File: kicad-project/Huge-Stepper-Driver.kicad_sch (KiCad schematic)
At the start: 0 parts

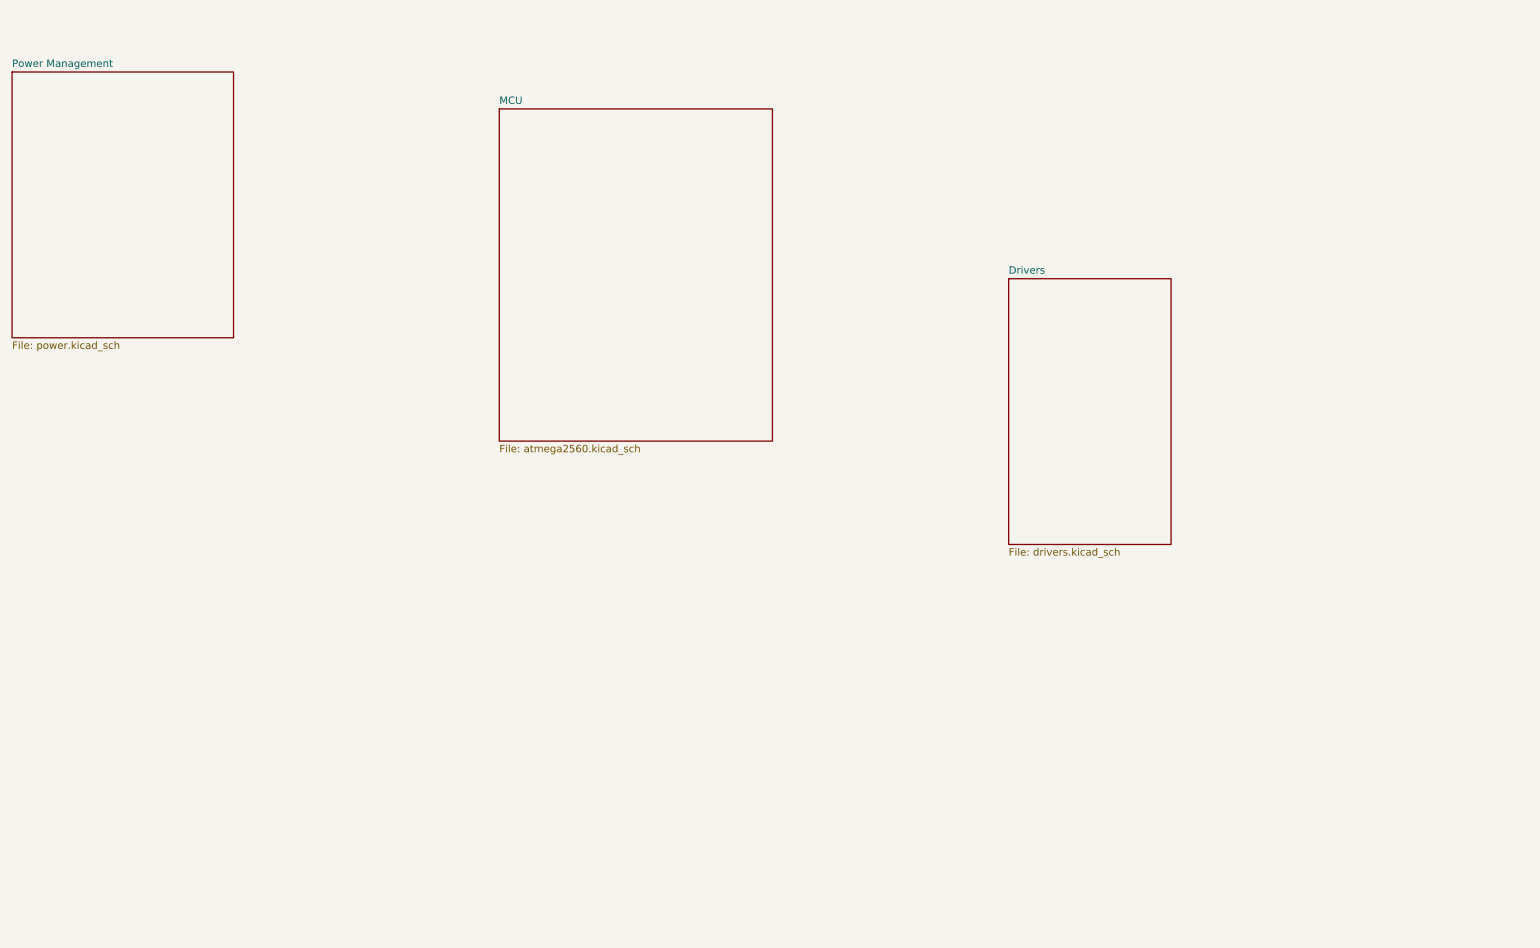
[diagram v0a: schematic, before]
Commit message: hw: rename poject and create project library
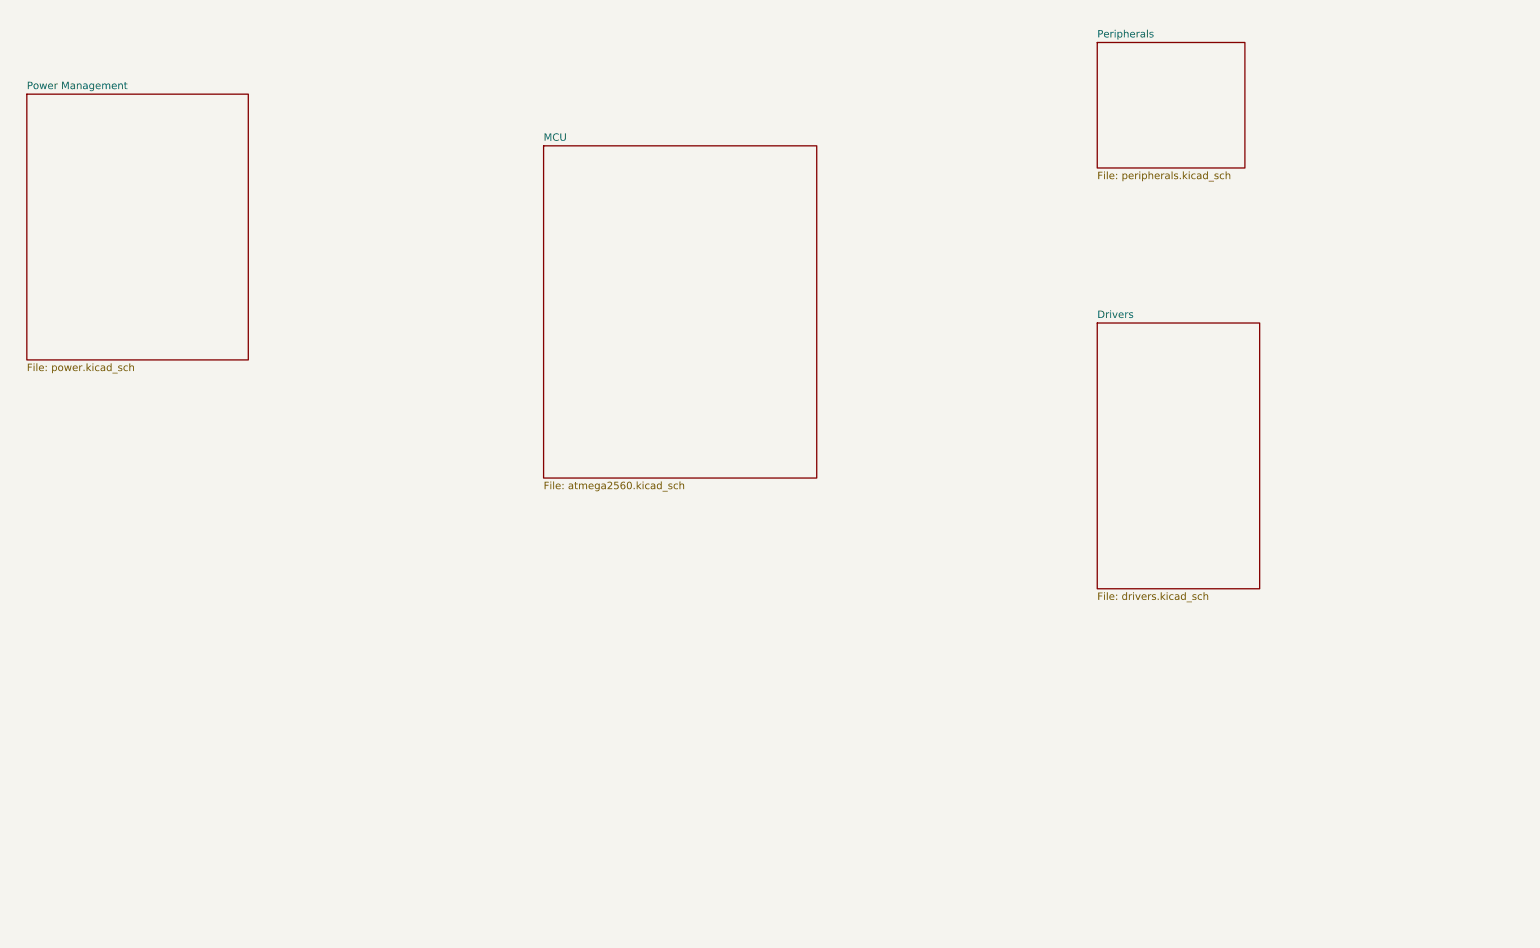
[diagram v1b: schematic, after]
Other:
- added sheet Peripherals (peripherals.kicad_sch)
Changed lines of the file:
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@@
 (kicad_sch (version 20211123) (generator eeschema)
   (paper "A4")
-  (sheet (at 119.38 52.07) (size 46.99 57.15) (fields_autoplaced)
-    (stroke (width 0.1524) (type solid) (color 0 0 0 0))
-    (fill (color 0 0 0 0.0000))
-    (property "Sheet name" "MCU" (id 0) (at 119.38 51.3584 0)
-      (effects (font (size 1.27 1.27)) (justify left bottom))
-    )
-    (property "Sheet file" "atmega2560.kicad_sch" (id 1) (at 119.38 109.8046 0)
-      (effects (font (size 1.27 1.27)) (justify left top))
-    )
-  )
-  (sheet (at 35.56 45.72) (size 38.1 45.72) (fields_autoplaced)
-    (stroke (width 0.1524) (type solid) (color 0 0 0 0))
-    (fill (color 0 0 0 0.0000))
-    (property "Sheet name" "Power Management" (id 0) (at 35.56 45.0084 0)
-      (effects (font (size 1.27 1.27)) (justify left bottom))
-    )
-    (property "Sheet file" "power.kicad_sch" (id 1) (at 35.56 92.0246 0)
-      (effects (font (size 1.27 1.27)) (justify left top))
-    )
-  )
-  (sheet (at 207.01 81.28) (size 27.94 45.72) (fields_autoplaced)
-    (stroke (width 0.1524) (type solid) (color 0 0 0 0))
-    (fill (color 0 0 0 0.0000))
-    (property "Sheet name" "Drivers" (id 0) (at 207.01 80.5684 0)
-      (effects (font (size 1.27 1.27)) (justify left bottom))
-    )
-    (property "Sheet file" "drivers.kicad_sch" (id 1) (at 207.01 127.5846 0)
+  (sheet (at 127 58.42) (size 46.99 57.15) (fields_autoplaced)
+    (stroke (width 0.1524) (type solid) (color 0 0 0 0))
+    (fill (color 0 0 0 0.0000))
+    (property "Sheet name" "MCU" (id 0) (at 127 57.7084 0)
+      (effects (font (size 1.27 1.27)) (justify left bottom))
+    )
+    (property "Sheet file" "atmega2560.kicad_sch" (id 1) (at 127 116.1546 0)
+      (effects (font (size 1.27 1.27)) (justify left top))
+    )
+  )
+  (sheet (at 222.25 40.64) (size 25.4 21.59) (fields_autoplaced)
+    (stroke (width 0.1524) (type solid) (color 0 0 0 0))
+    (fill (color 0 0 0 0.0000))
+    (property "Sheet name" "Peripherals" (id 0) (at 222.25 39.9284 0)
+      (effects (font (size 1.27 1.27)) (justify left bottom))
+    )
+    (property "Sheet file" "peripherals.kicad_sch" (id 1) (at 222.25 62.8146 0)
+      (effects (font (size 1.27 1.27)) (justify left top))
+    )
+  )
+  (sheet (at 38.1 49.53) (size 38.1 45.72) (fields_autoplaced)
+    (stroke (width 0.1524) (type solid) (color 0 0 0 0))
+    (fill (color 0 0 0 0.0000))
+    (property "Sheet name" "Power Management" (id 0) (at 38.1 48.8184 0)
+      (effects (font (size 1.27 1.27)) (justify left bottom))
+    )
+    (property "Sheet file" "power.kicad_sch" (id 1) (at 38.1 95.8346 0)
+      (effects (font (size 1.27 1.27)) (justify left top))
+    )
+  )
+  (sheet (at 222.25 88.9) (size 27.94 45.72) (fields_autoplaced)
+    (stroke (width 0.1524) (type solid) (color 0 0 0 0))
+    (fill (color 0 0 0 0.0000))
+    (property "Sheet name" "Drivers" (id 0) (at 222.25 88.1884 0)
+      (effects (font (size 1.27 1.27)) (justify left bottom))
+    )
+    (property "Sheet file" "drivers.kicad_sch" (id 1) (at 222.25 135.2046 0)
       (effects (font (size 1.27 1.27)) (justify left top))
     )
@@
     (path "/f5d928fb-e6dd-4010-8c57-6f8716fdab33" (page "3"))
     (path "/4f8c7c93-1d61-4a01-a5c2-288dd81060c9" (page "4"))
+    (path "/3d25ea00-3597-4b84-9896-d06c9254cef7" (page "5"))
   )
   (symbol_instances
@@
       (reference "#PWR?") (unit 1) (value "+5V") (footprint "")
     )
+    (path "/f5d928fb-e6dd-4010-8c57-6f8716fdab33/25a53107-0414-4363-9616-a7d291dc0d84"
+      (reference "#PWR?") (unit 1) (value "+12V") (footprint "")
+    )
     (path "/f5d928fb-e6dd-4010-8c57-6f8716fdab33/2942b730-6142-444d-941a-095db45b9805"
       (reference "#PWR?") (unit 1) (value "GND") (footprint "")
@@
       (reference "#PWR?") (unit 1) (value "+5V") (footprint "")
     )
+    (path "/3d25ea00-3597-4b84-9896-d06c9254cef7/4c436fb9-5de1-4241-82c9-60c46b745983"
+      (reference "#PWR?") (unit 1) (value "GND") (footprint "")
+    )
+    (path "/3d25ea00-3597-4b84-9896-d06c9254cef7/53eb5fc0-41cc-43ad-8003-3a7163adca82"
+      (reference "#PWR?") (unit 1) (value "GND") (footprint "")
+    )
+    (path "/3d25ea00-3597-4b84-9896-d06c9254cef7/5b7004c0-970a-4c32-afa1-b9c30b457ebb"
+      (reference "#PWR?") (unit 1) (value "GND") (footprint "")
+    )
     (path "/f5d928fb-e6dd-4010-8c57-6f8716fdab33/5f7cd6da-1976-40d7-8175-57317f64748c"
       (reference "#PWR?") (unit 1) (value "GND") (footprint "")
     )
+    (path "/3d25ea00-3597-4b84-9896-d06c9254cef7/756c57ca-b724-416e-bbc3-080fcadffb70"
+      (reference "#PWR?") (unit 1) (value "GND") (footprint "")
+    )
+    (path "/f5d928fb-e6dd-4010-8c57-6f8716fdab33/9a7047f9-acea-486f-a364-b7368cdd257a"
+      (reference "#PWR?") (unit 1) (value "+12V") (footprint "")
+    )
     (path "/18df3b4d-b69d-45aa-8b2a-e433af4ece2d/a7d63353-8f9e-4f12-a0a0-581ff55f9e74"
       (reference "#PWR?") (unit 1) (value "GND") (footprint "")
     )
+    (path "/3d25ea00-3597-4b84-9896-d06c9254cef7/aede887e-5713-4410-b301-8003185f738f"
+      (reference "#PWR?") (unit 1) (value "GND") (footprint "")
+    )
     (path "/f5d928fb-e6dd-4010-8c57-6f8716fdab33/bd1d99b9-625b-4d9f-8b97-620535fb200d"
       (reference "#PWR?") (unit 1) (value "GND") (footprint "")
+    )
+    (path "/3d25ea00-3597-4b84-9896-d06c9254cef7/c6a9b2da-bd30-4983-ad00-dc03e640a581"
+      (reference "#PWR?") (unit 1) (value "+3V3") (footprint "")
+    )
+    (path "/3d25ea00-3597-4b84-9896-d06c9254cef7/cefd0a94-cc8a-494c-9a46-c853604e1e17"
+      (reference "#PWR?") (unit 1) (value "+3V3") (footprint "")
+    )
+    (path "/3d25ea00-3597-4b84-9896-d06c9254cef7/d190d7a3-7bf5-42db-8c6f-15b2790a1189"
+      (reference "#PWR?") (unit 1) (value "GND") (footprint "")
+    )
+    (path "/3d25ea00-3597-4b84-9896-d06c9254cef7/e22a8115-21c4-4079-b548-13d39057d641"
+      (reference "#PWR?") (unit 1) (value "+3V3") (footprint "")
     )
     (path "/f5d928fb-e6dd-4010-8c57-6f8716fdab33/e24fb780-68ae-495b-a949-7ef7931dd25d"
@@
       (reference "#PWR?") (unit 1) (value "GND") (footprint "")
     )
+    (path "/3d25ea00-3597-4b84-9896-d06c9254cef7/80dec395-b03d-42e4-894e-d6e2d9479fc8"
+      (reference "BZ?") (unit 1) (value "Buzzer") (footprint "Buzzer_Beeper:Buzzer_12x9.5RM7.6")
+    )
     (path "/f5d928fb-e6dd-4010-8c57-6f8716fdab33/38c76cd1-d3ed-4a45-9878-1458ed9b04ed"
       (reference "C?") (unit 1) (value "0.1u") (footprint "")
@@
       (reference "C?") (unit 1) (value "0.1u") (footprint "")
     )
+    (path "/3d25ea00-3597-4b84-9896-d06c9254cef7/716e5416-b330-423a-811f-046a4ee64f5e"
+      (reference "D?") (unit 1) (value "GREEN_LED") (footprint "LED_SMD:LED_0603_1608Metric")
+    )
+    (path "/3d25ea00-3597-4b84-9896-d06c9254cef7/e30e2336-2dbc-4130-9889-d5f2eae65709"
+      (reference "D?") (unit 1) (value "LED_RGB") (footprint "LED_SMD:LED_RGB_1210")
+    )
     (path "/4f8c7c93-1d61-4a01-a5c2-288dd81060c9/41d2c036-0133-4858-af37-ae05a7f175e8"
       (reference "H?") (unit 1) (value "MountingHole") (footprint "")
@@
       (reference "J?") (unit 1) (value "Screw_Terminal_01x02") (footprint "")
     )
+    (path "/3d25ea00-3597-4b84-9896-d06c9254cef7/4e3ce3b2-0062-4894-90c9-d123f1516483"
+      (reference "J?") (unit 1) (value "Conn_01x04") (footprint "Connector_PinHeader_2.54mm:PinHeader_1x04_P2.54mm_Vertical_SMD_Pin1Left")
+    )
+    (path "/f5d928fb-e6dd-4010-8c57-6f8716fdab33/70d8d5c4-6ca3-4d9d-b0ee-1b92bdb07be0"
+      (reference "J?") (unit 1) (value "Screw_Terminal_01x05") (footprint "TerminalBlock_TE-Connectivity:TerminalBlock_TE_282834-5_1x05_P2.54mm_Horizontal")
+    )
+    (path "/f5d928fb-e6dd-4010-8c57-6f8716fdab33/9e493dfe-75da-48fa-ad61-eaa217b673f3"
+      (reference "J?") (unit 1) (value "Screw_Terminal_01x05") (footprint "TerminalBlock_TE-Connectivity:TerminalBlock_TE_282834-5_1x05_P2.54mm_Horizontal")
+    )
+    (path "/3d25ea00-3597-4b84-9896-d06c9254cef7/b93ddd20-6b06-4f50-a42d-38095b2ae703"
+      (reference "Q?") (unit 1) (value "PDTC114Y") (footprint "")
+    )
     (path "/f5d928fb-e6dd-4010-8c57-6f8716fdab33/37dac4eb-1daa-4fa2-a92f-452234732f13"
       (reference "R?") (unit 1) (value "R") (footprint "")
     )
+    (path "/3d25ea00-3597-4b84-9896-d06c9254cef7/3a40cb9a-6096-4b48-bae2-62ca7cd7dbcd"
+      (reference "R?") (unit 1) (value "R") (footprint "Resistor_SMD:R_0603_1608Metric")
+    )
     (path "/f5d928fb-e6dd-4010-8c57-6f8716fdab33/3e5f1652-1224-4863-9681-d782bc9660ba"
       (reference "R?") (unit 1) (value "5k") (footprint "")
     )
+    (path "/3d25ea00-3597-4b84-9896-d06c9254cef7/476016a1-85a2-490a-9e22-631280b45f0e"
+      (reference "R?") (unit 1) (value "4k7") (footprint "Resistor_SMD:R_0603_1608Metric")
+    )
     (path "/f5d928fb-e6dd-4010-8c57-6f8716fdab33/62c00295-c371-40ec-97e2-435adbc65cbd"
       (reference "R?") (unit 1) (value "R") (footprint "")
     )
+    (path "/3d25ea00-3597-4b84-9896-d06c9254cef7/86c06a99-e0bc-40d5-a7f9-e5b1bfafe6eb"
+      (reference "R?") (unit 1) (value "R") (footprint "Resistor_SMD:R_0603_1608Metric")
+    )
+    (path "/3d25ea00-3597-4b84-9896-d06c9254cef7/a174e5fd-6a2e-44e2-8acc-20c14c8a9718"
+      (reference "R?") (unit 1) (value "330") (footprint "Resistor_SMD:R_0603_1608Metric")
+    )
     (path "/f5d928fb-e6dd-4010-8c57-6f8716fdab33/ce3284f3-a343-4acc-ac4c-24b15f7cfe2f"
       (reference "R?") (unit 1) (value "R") (footprint "")
     )
+    (path "/3d25ea00-3597-4b84-9896-d06c9254cef7/cfd66066-4bfb-415b-aff3-80ee08e719fe"
+      (reference "R?") (unit 1) (value "R") (footprint "Resistor_SMD:R_0603_1608Metric")
+    )
     (path "/18df3b4d-b69d-45aa-8b2a-e433af4ece2d/449c8645-e2fc-4ff8-89d1-ec8245776958"

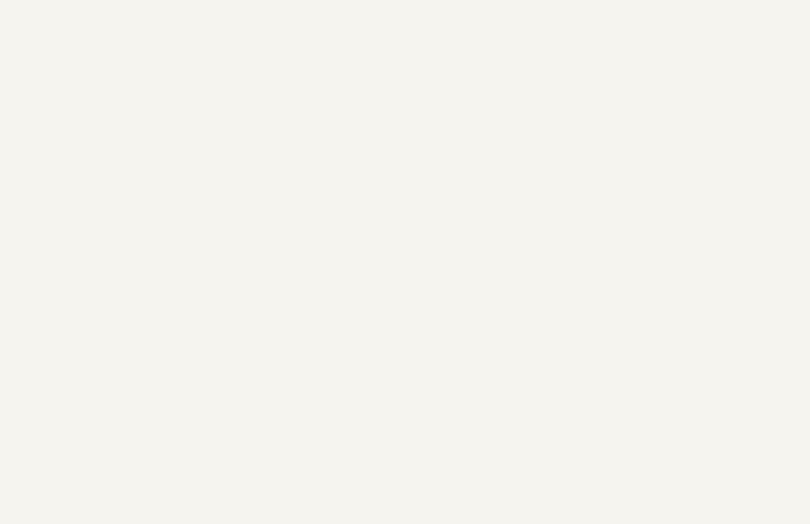
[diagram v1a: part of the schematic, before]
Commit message: hw: add power managment
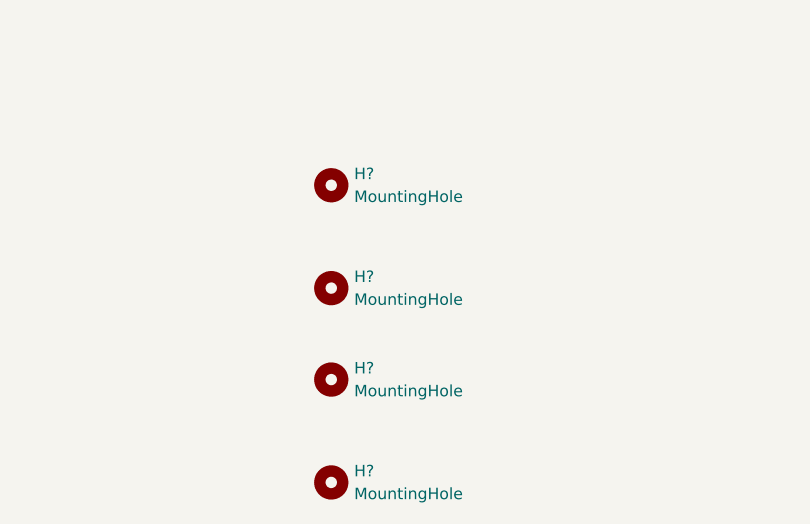
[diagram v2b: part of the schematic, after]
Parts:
- added H? (x4): MountingHole, symbol Mechanical:MountingHole

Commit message: hw: update
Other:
- sheet Drivers renamed Bipolar Driver 1
- added sheet Unipolar Driver  (unipolar.kicad_sch)

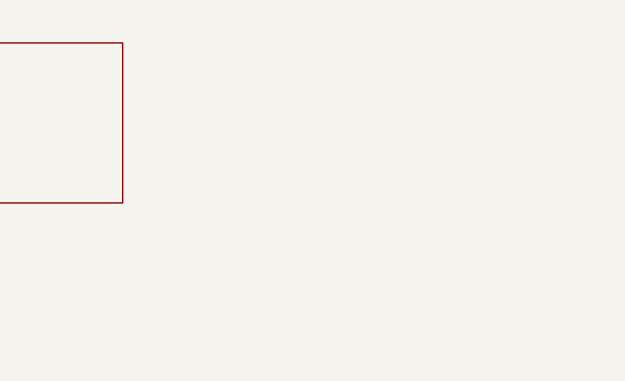
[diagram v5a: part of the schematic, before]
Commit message: hw: change power management and drivers
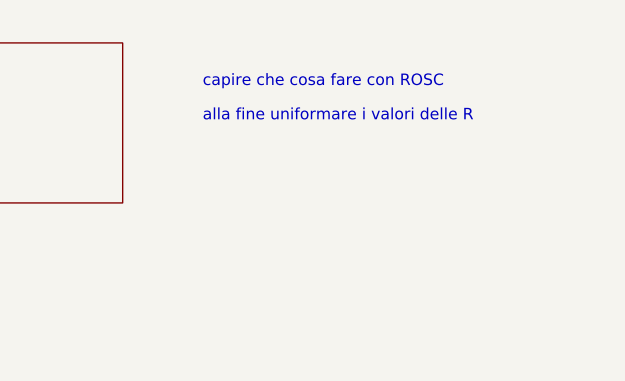
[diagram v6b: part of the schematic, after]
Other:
- note added: "alla fine uniformare i valori delle R"
- note added: "capire che cosa fare con ROSC"

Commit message: hw: update to complete schematic
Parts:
- gave numbers to parts that had none: 4
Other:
- sheet Bipolar Driver 1 renamed Bipolar Drivers
- sheet Bipolar Drivers ports: added DIR_A, DIR_B, DIR_C, DIR_D, EN_MOTORS, STEP_A, STEP_B, STEP_C, STEP_D; removed none
- sheet MCU ports: added BUZZER, DIR_A, DIR_B, DIR_C, DIR_D, EN_MOTORS, ESP_RX, ESP_TX, I2C_SCL, I2C_SDA, LED_B, LED_G, LED_R, LS1, LS2, LS3, LS4, ME_W11, ME_W12, ME_W21, ME_W22, STEP_A, STEP_B, STEP_C, STEP_D, USB_D+, USB_D-; removed none
- sheet Peripherals ports: added BUZZER, ESP_RX, ESP_TX, I2C_SCL, I2C_SDA, LED_B, LED_G, LED_R, LS1, LS2, LS3, LS4; removed none
- sheet Power Management ports: added USB_D+, USB_D-; removed none
- sheet Unipolar Driver  ports: added ME_W11, ME_W12, ME_W21, ME_W22; removed none
- note removed: "alla fine uniformare i valori delle R"
- note removed: "capire che cosa fare con ROSC"
